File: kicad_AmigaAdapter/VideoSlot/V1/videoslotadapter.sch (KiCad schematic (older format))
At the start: 16 parts, among them U1 74LVC86, U2 74LVC574, U3 74LVC574, U4 TLV74333PDBVR, U5 74LVC86

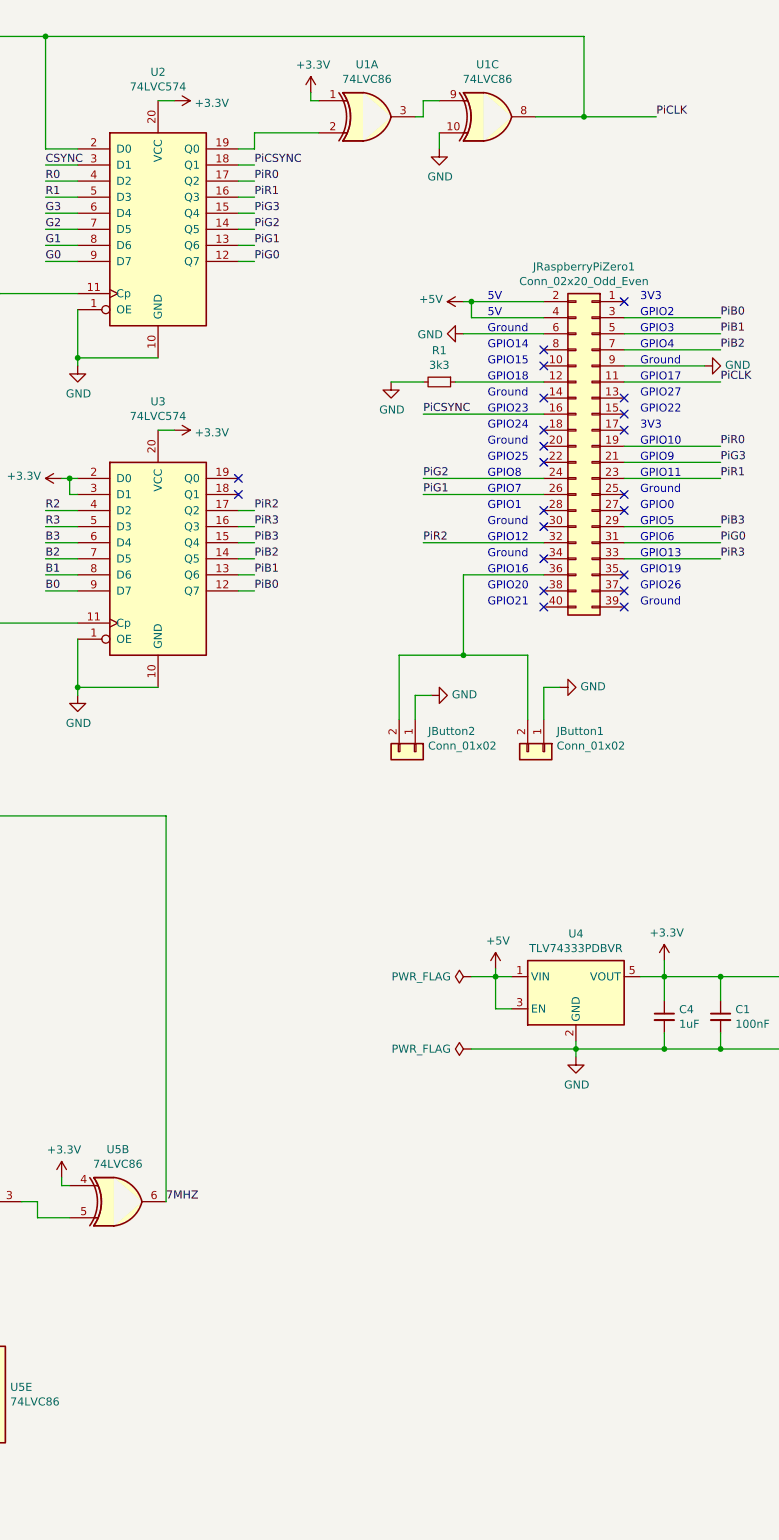
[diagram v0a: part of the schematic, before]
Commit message: V1.01 layout updates to inlcude 47pf capacitor, ground extra floating pins on U5
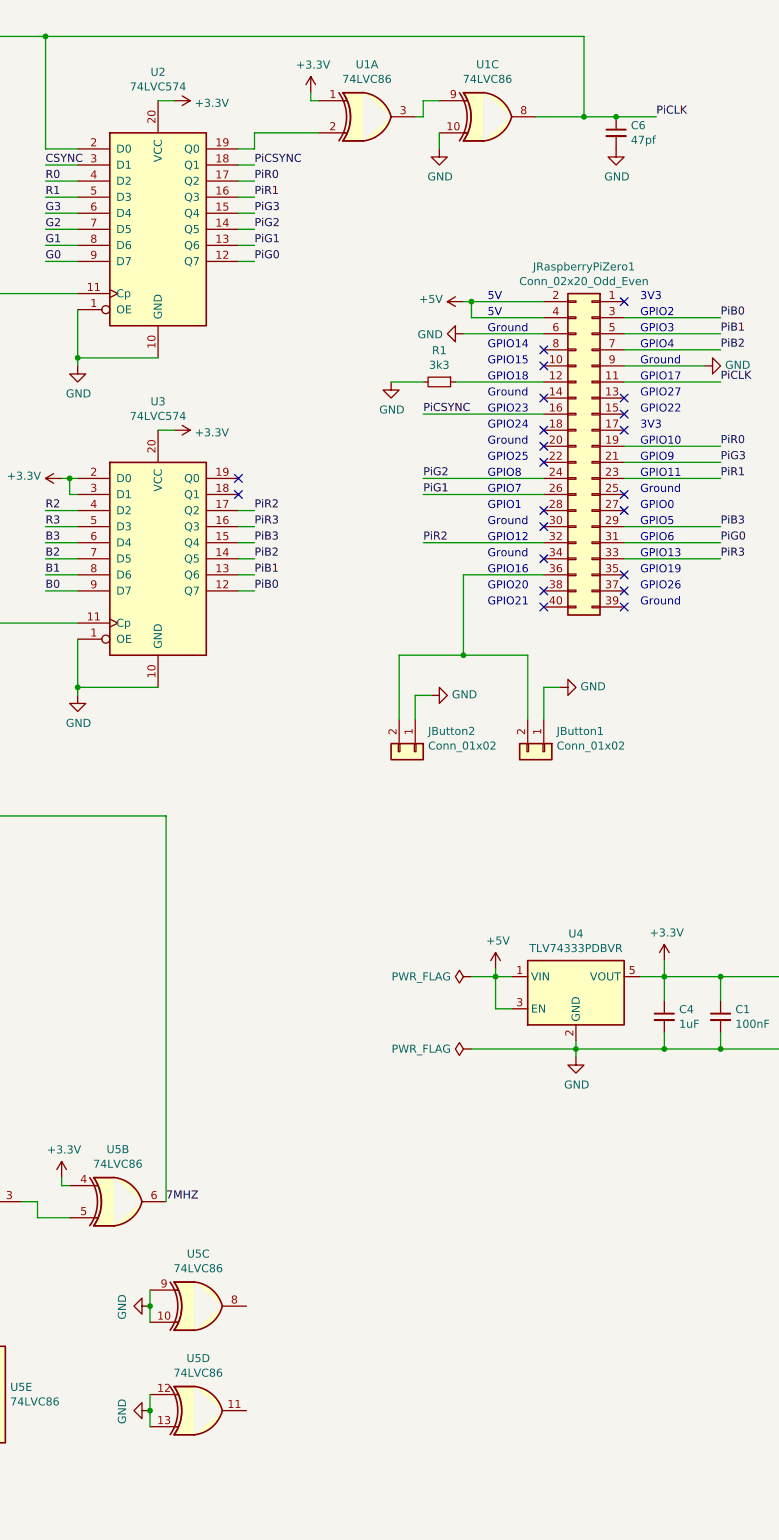
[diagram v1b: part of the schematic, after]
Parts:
- added C6: 47pf, Capacitor_SMD:C_0603_1608Metric_Pad1.05x0.95mm_HandSolder, symbol Device:C_Small
- added unit 3 of U5
- added unit 4 of U5
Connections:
- net GND: now also C6.2, U5.10, U5.12, U5.13, U5.9
- net PiCLK: now also C6.1
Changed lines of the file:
@@
 Sheet 1 1
 Title "RGBtoHDMI Amiga Video Slot Adapter"
-Date "2021-02-06"
-Rev "1"
+Date "2021-04-03"
+Rev "1.01"
 Comp ""
 Comment1 ""
@@
 Connection ~ 9050 1500
 Wire Wire Line
-	9050 1500 9500 1500
+	9050 1500 9250 1500
 $Comp
 L power:GND #PWR0108
@@
 Text Label 4950 8150 2    50   ~ 0
 C1
+$Comp
+L Device:C_Small C6
+U 1 1 60693B85
+P 9250 1600
+F 0 "C6" H 9342 1646 50  0000 L CNN
+F 1 "47pf" H 9342 1555 50  0000 L CNN
+F 2 "Capacitor_SMD:C_0603_1608Metric_Pad1.05x0.95mm_HandSolder" H 9250 1600 50  0001 C CNN
+F 3 "~" H 9250 1600 50  0001 C CNN
+	1    9250 1600
+	1    0    0    -1
+$EndComp
+Connection ~ 9250 1500
+Wire Wire Line
+	9250 1500 9500 1500
+$Comp
+L power:GND #PWR0125
+U 1 1 606959B9
+P 9250 1700
+F 0 "#PWR0125" H 9250 1450 50  0001 C CNN
+F 1 "GND" H 9255 1527 50  0000 C CNN
+F 2 "" H 9250 1700 50  0001 C CNN
+F 3 "" H 9250 1700 50  0001 C CNN
+	1    9250 1700
+	1    0    0    -1
+$EndComp
+$Comp
+L 74xx:74HC86 U5
+U 3 1 606D7CDB
+P 6650 8900
+F 0 "U5" H 6650 9225 50  0000 C CNN
+F 1 "74LVC86" H 6650 9134 50  0000 C CNN
+F 2 "Package_SO:TSSOP-14_4.4x5mm_P0.65mm" H 6650 8900 50  0001 C CNN
+F 3 "http://www.ti.com/lit/gpn/sn74HC86" H 6650 8900 50  0001 C CNN
+	3    6650 8900
+	1    0    0    -1
+$EndComp
+$Comp
+L 74xx:74HC86 U5
+U 4 1 606DDCCA
+P 6650 9550
+F 0 "U5" H 6650 9875 50  0000 C CNN
+F 1 "74LVC86" H 6650 9784 50  0000 C CNN
+F 2 "Package_SO:TSSOP-14_4.4x5mm_P0.65mm" H 6650 9550 50  0001 C CNN
+F 3 "http://www.ti.com/lit/gpn/sn74HC86" H 6650 9550 50  0001 C CNN
+	4    6650 9550
+	1    0    0    -1
+$EndComp
+Wire Wire Line
+	6350 8800 6350 8900
+Wire Wire Line
+	6350 9450 6350 9550
+$Comp
+L power:GND #PWR0126
+U 1 1 60701548
+P 6350 8900
+F 0 "#PWR0126" H 6350 8650 50  0001 C CNN
+F 1 "GND" H 6355 8727 50  0000 C CNN
+F 2 "" H 6350 8900 50  0001 C CNN
+F 3 "" H 6350 8900 50  0001 C CNN
+	1    6350 8900
+	0    1    1    0
+$EndComp
+Connection ~ 6350 8900
+Wire Wire Line
+	6350 8900 6350 9000
+$Comp
+L power:GND #PWR0127
+U 1 1 60715844
+P 6350 9550
+F 0 "#PWR0127" H 6350 9300 50  0001 C CNN
+F 1 "GND" H 6355 9377 50  0000 C CNN
+F 2 "" H 6350 9550 50  0001 C CNN
+F 3 "" H 6350 9550 50  0001 C CNN
+	1    6350 9550
+	0    1    1    0
+$EndComp
+Connection ~ 6350 9550
+Wire Wire Line
+	6350 9550 6350 9650
 $EndSCHEMATC

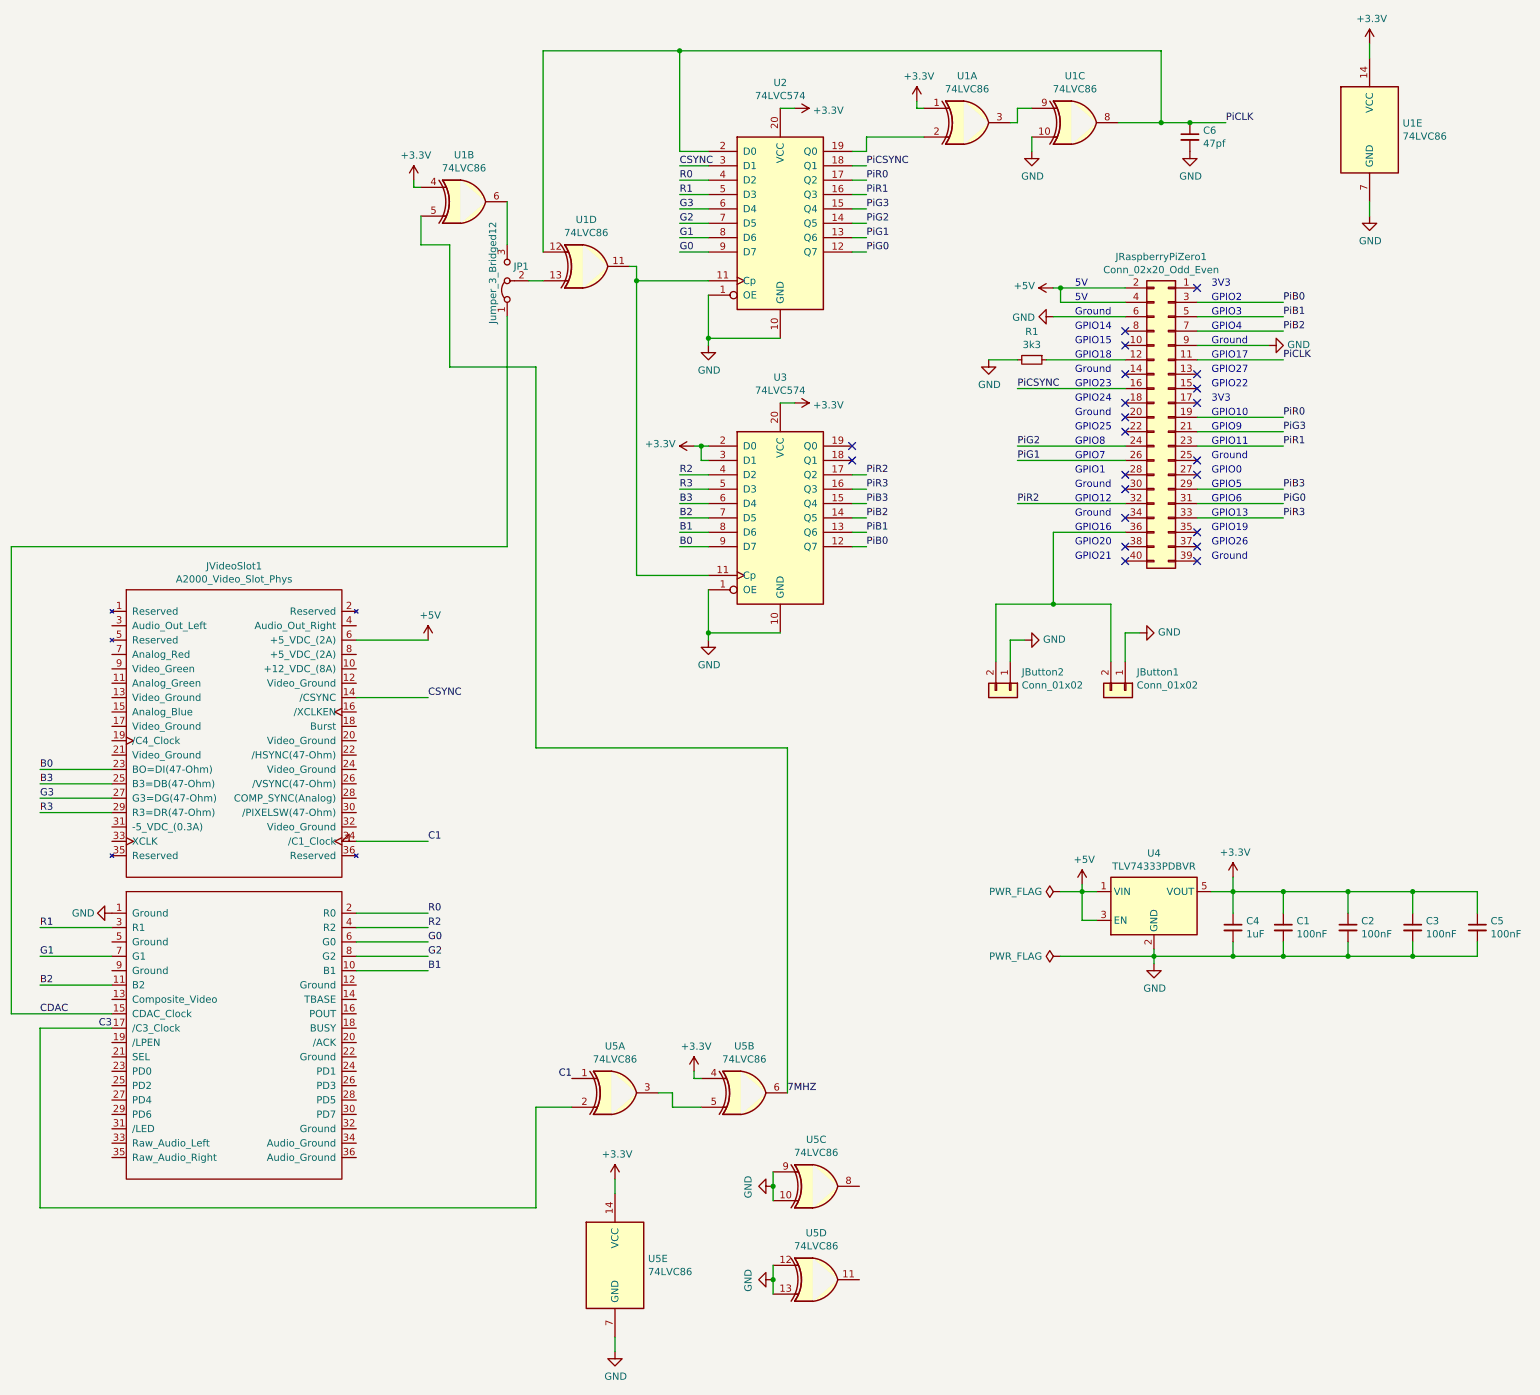
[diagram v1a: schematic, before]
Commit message: V1.1 Updates to improve picture quality and eliminate the need for excessive overclocking
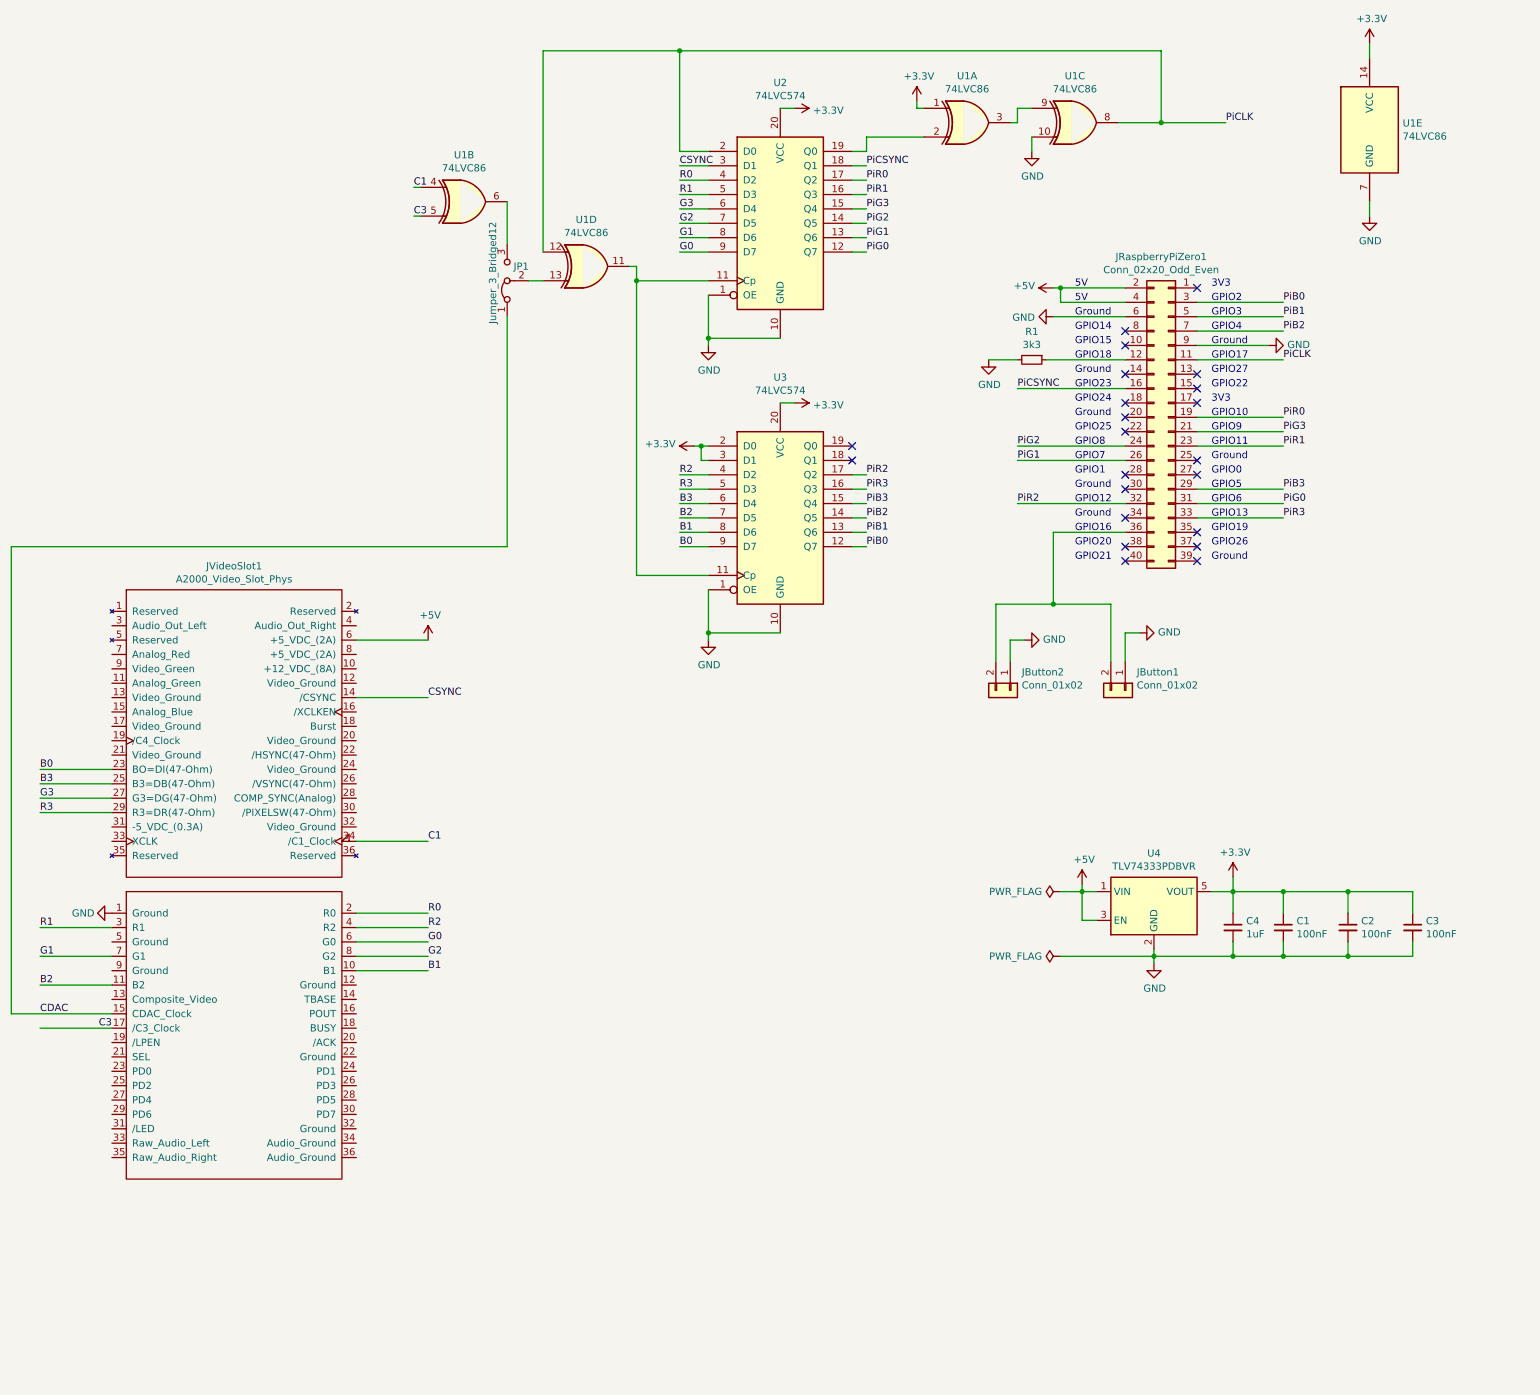
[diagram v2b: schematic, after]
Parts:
- removed C5: 100nF, Capacitor_SMD:C_0603_1608Metric_Pad1.05x0.95mm_HandSolder, symbol Device:C_Small
- removed C6: 47pf, Capacitor_SMD:C_0603_1608Metric_Pad1.05x0.95mm_HandSolder, symbol Device:C_Small
- removed U5: 74LVC86, Package_SO:TSSOP-14_4.4x5mm_P0.65mm, symbol 74xx:74HC86
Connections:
- net 7MHZ is gone; now on net C3: U1.5
- net +3V3: no longer U1.4
- net C1: now also U1.4
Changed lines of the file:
@@
 Sheet 1 1
 Title "RGBtoHDMI Amiga Video Slot Adapter"
-Date "2021-04-03"
-Rev "1.01"
+Date "2021-06-03"
+Rev "1.1"
 Comp ""
 Comment1 ""
@@
 	9050 1500 9050 1000
 Connection ~ 9050 1500
-Wire Wire Line
-	9050 1500 9250 1500
 $Comp
 L power:GND #PWR0108
@@
 Wire Wire Line
 	8150 1700 8150 1600
-Text Label 6450 8250 0    50   ~ 0
-7MHZ
 Wire Wire Line
 	5350 2500 5400 2500
@@
 Wire Wire Line
 	4500 2350 4500 2050
-Wire Wire Line
-	4100 2350 3900 2350
-Wire Wire Line
-	3900 2350 3900 2150
-$Comp
-L power:+3.3V #PWR0110
-U 1 1 5F7C63B6
-P 3850 1900
-F 0 "#PWR0110" H 3850 1750 50  0001 C CNN
-F 1 "+3.3V" H 3865 2073 50  0000 C CNN
-F 2 "" H 3850 1900 50  0001 C CNN
-F 3 "" H 3850 1900 50  0001 C CNN
-	1    3850 1900
-	1    0    0    -1
-$EndComp
-Wire Wire Line
-	3850 1900 3850 1950
 Wire Wire Line
 	3850 1950 3900 1950
@@
 	1050 7700 1750 7700
 $Comp
-L 74xx:74HC86 U5
-U 2 1 604D47AE
-P 6150 8250
-F 0 "U5" H 6150 8575 50  0000 C CNN
-F 1 "74LVC86" H 6150 8484 50  0000 C CNN
-F 2 "Package_SO:TSSOP-14_4.4x5mm_P0.65mm" H 6150 8250 50  0001 C CNN
-F 3 "http://www.ti.com/lit/gpn/sn74HC86" H 6150 8250 50  0001 C CNN
-	2    6150 8250
-	1    0    0    -1
-$EndComp
-$Comp
-L power:+3.3V #PWR0111
-U 1 1 604D47B5
-P 5800 8100
-F 0 "#PWR0111" H 5800 7950 50  0001 C CNN
-F 1 "+3.3V" H 5815 8273 50  0000 C CNN
-F 2 "" H 5800 8100 50  0001 C CNN
-F 3 "" H 5800 8100 50  0001 C CNN
-	1    5800 8100
-	1    0    0    -1
-$EndComp
-Wire Wire Line
-	5800 8100 5800 8150
-Wire Wire Line
-	5800 8150 5850 8150
-$Comp
-L 74xx:74HC86 U5
-U 1 1 604E2976
-P 5250 8250
-F 0 "U5" H 5250 8575 50  0000 C CNN
-F 1 "74LVC86" H 5250 8484 50  0000 C CNN
-F 2 "Package_SO:TSSOP-14_4.4x5mm_P0.65mm" H 5250 8250 50  0001 C CNN
-F 3 "http://www.ti.com/lit/gpn/sn74HC86" H 5250 8250 50  0001 C CNN
-	1    5250 8250
-	1    0    0    -1
-$EndComp
-Wire Wire Line
-	1250 7800 1250 9050
-Wire Wire Line
-	1250 9050 4700 9050
-Wire Wire Line
-	4700 9050 4700 8350
-Wire Wire Line
-	4700 8350 4950 8350
-Wire Wire Line
-	5650 8350 5650 8250
-Wire Wire Line
-	5550 8250 5650 8250
-Wire Wire Line
-	5650 8350 5850 8350
-Wire Wire Line
-	6450 8250 6450 5850
-Wire Wire Line
-	6450 5850 4700 5850
-Wire Wire Line
-	4700 5850 4700 3200
-Wire Wire Line
-	4700 3200 4100 3200
-Wire Wire Line
-	4100 2350 4100 3200
-$Comp
-L 74xx:74HC86 U5
-U 5 1 605A5914
-P 5250 9450
-F 0 "U5" H 5480 9496 50  0000 L CNN
-F 1 "74LVC86" H 5480 9405 50  0000 L CNN
-F 2 "Package_SO:TSSOP-14_4.4x5mm_P0.65mm" H 5250 9450 50  0001 C CNN
-F 3 "http://www.ti.com/lit/gpn/sn74HC86" H 5250 9450 50  0001 C CNN
-	5    5250 9450
-	1    0    0    -1
-$EndComp
-$Comp
-L power:GND #PWR0116
-U 1 1 605A591A
-P 5250 10050
-F 0 "#PWR0116" H 5250 9800 50  0001 C CNN
-F 1 "GND" H 5255 9877 50  0000 C CNN
-F 2 "" H 5250 10050 50  0001 C CNN
-F 3 "" H 5250 10050 50  0001 C CNN
-	1    5250 10050
-	1    0    0    -1
-$EndComp
-$Comp
-L power:+3.3V #PWR0118
-U 1 1 605A5920
-P 5250 8850
-F 0 "#PWR0118" H 5250 8700 50  0001 C CNN
-F 1 "+3.3V" H 5265 9023 50  0000 C CNN
-F 2 "" H 5250 8850 50  0001 C CNN
-F 3 "" H 5250 8850 50  0001 C CNN
-	1    5250 8850
-	1    0    0    -1
-$EndComp
-Wire Wire Line
-	5250 8850 5250 8950
-Wire Wire Line
-	5250 9950 5250 10050
-$Comp
-L Device:C_Small C5
-U 1 1 605D70A1
-P 11250 7100
-F 0 "C5" H 11342 7146 50  0000 L CNN
-F 1 "100nF" H 11342 7055 50  0000 L CNN
-F 2 "Capacitor_SMD:C_0603_1608Metric_Pad1.05x0.95mm_HandSolder" H 11250 7100 50  0001 C CNN
-F 3 "~" H 11250 7100 50  0001 C CNN
-	1    11250 7100
-	1    0    0    -1
-$EndComp
-Wire Wire Line
-	10800 6850 11250 6850
-Wire Wire Line
-	11250 6850 11250 7000
-Wire Wire Line
-	11250 7200 11250 7300
-Wire Wire Line
-	11250 7300 10800 7300
-Connection ~ 10800 6850
-Connection ~ 10800 7300
-$Comp
 L Connector_Generic:Conn_01x02 JButton2
 U 1 1 605EA3DB
@@
 Wire Wire Line
 	3450 6500 3950 6500
-Text Label 4950 8150 2    50   ~ 0
+Text Label 3850 1950 0    50   ~ 0
 C1
-$Comp
-L Device:C_Small C6
-U 1 1 60693B85
-P 9250 1600
-F 0 "C6" H 9342 1646 50  0000 L CNN
-F 1 "47pf" H 9342 1555 50  0000 L CNN
-F 2 "Capacitor_SMD:C_0603_1608Metric_Pad1.05x0.95mm_HandSolder" H 9250 1600 50  0001 C CNN
-F 3 "~" H 9250 1600 50  0001 C CNN
-	1    9250 1600
-	1    0    0    -1
-$EndComp
-Connection ~ 9250 1500
-Wire Wire Line
-	9250 1500 9500 1500
-$Comp
-L power:GND #PWR0125
-U 1 1 606959B9
-P 9250 1700
-F 0 "#PWR0125" H 9250 1450 50  0001 C CNN
-F 1 "GND" H 9255 1527 50  0000 C CNN
-F 2 "" H 9250 1700 50  0001 C CNN
-F 3 "" H 9250 1700 50  0001 C CNN
-	1    9250 1700
-	1    0    0    -1
-$EndComp
-$Comp
-L 74xx:74HC86 U5
-U 3 1 606D7CDB
-P 6650 8900
-F 0 "U5" H 6650 9225 50  0000 C CNN
-F 1 "74LVC86" H 6650 9134 50  0000 C CNN
-F 2 "Package_SO:TSSOP-14_4.4x5mm_P0.65mm" H 6650 8900 50  0001 C CNN
-F 3 "http://www.ti.com/lit/gpn/sn74HC86" H 6650 8900 50  0001 C CNN
-	3    6650 8900
-	1    0    0    -1
-$EndComp
-$Comp
-L 74xx:74HC86 U5
-U 4 1 606DDCCA
-P 6650 9550
-F 0 "U5" H 6650 9875 50  0000 C CNN
-F 1 "74LVC86" H 6650 9784 50  0000 C CNN
-F 2 "Package_SO:TSSOP-14_4.4x5mm_P0.65mm" H 6650 9550 50  0001 C CNN
-F 3 "http://www.ti.com/lit/gpn/sn74HC86" H 6650 9550 50  0001 C CNN
-	4    6650 9550
-	1    0    0    -1
-$EndComp
-Wire Wire Line
-	6350 8800 6350 8900
-Wire Wire Line
-	6350 9450 6350 9550
-$Comp
-L power:GND #PWR0126
-U 1 1 60701548
-P 6350 8900
-F 0 "#PWR0126" H 6350 8650 50  0001 C CNN
-F 1 "GND" H 6355 8727 50  0000 C CNN
-F 2 "" H 6350 8900 50  0001 C CNN
-F 3 "" H 6350 8900 50  0001 C CNN
-	1    6350 8900
-	0    1    1    0
-$EndComp
-Connection ~ 6350 8900
-Wire Wire Line
-	6350 8900 6350 9000
-$Comp
-L power:GND #PWR0127
-U 1 1 60715844
-P 6350 9550
-F 0 "#PWR0127" H 6350 9300 50  0001 C CNN
-F 1 "GND" H 6355 9377 50  0000 C CNN
-F 2 "" H 6350 9550 50  0001 C CNN
-F 3 "" H 6350 9550 50  0001 C CNN
-	1    6350 9550
-	0    1    1    0
-$EndComp
-Connection ~ 6350 9550
-Wire Wire Line
-	6350 9550 6350 9650
+Wire Wire Line
+	3900 2150 3850 2150
+Text Label 3850 2150 0    50   ~ 0
+C3
+Wire Wire Line
+	9050 1500 9500 1500
 $EndSCHEMATC
